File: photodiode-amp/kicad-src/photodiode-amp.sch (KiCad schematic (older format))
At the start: 10 parts, among them J2 Conn_01x04, U1 OPA333xxDBV

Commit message: creates pd amp prod files
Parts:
- gave numbers to parts that had none: 1
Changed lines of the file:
@@
 $EndComp
 $Comp
-L Sensor_Optical:BPX61 D?
+L Sensor_Optical:BPX61 D1
 U 1 1 61B6A38B
 P 5325 2575
-F 0 "D?" V 5321 2497 50  0000 R CNN
+F 0 "D1" V 5321 2497 50  0000 R CNN
 F 1 "BPX61" V 5230 2497 50  0000 R CNN
 F 2 "Package_TO_SOT_THT:TO-5-2_Window" H 5325 2750 50  0001 C CNN

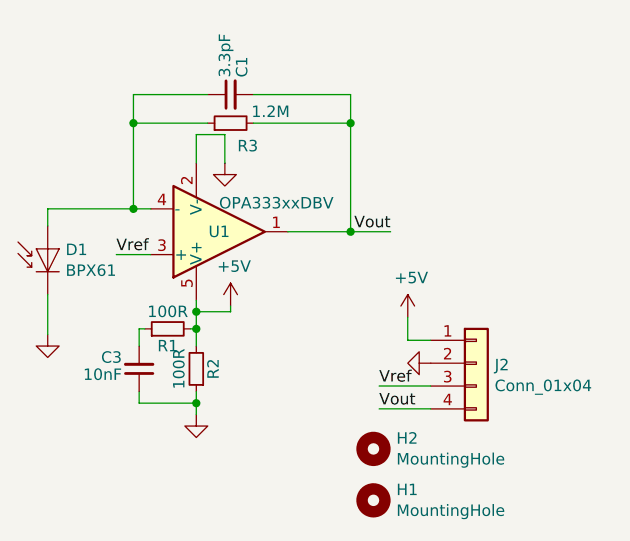
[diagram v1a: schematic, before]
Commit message: update component values and ids
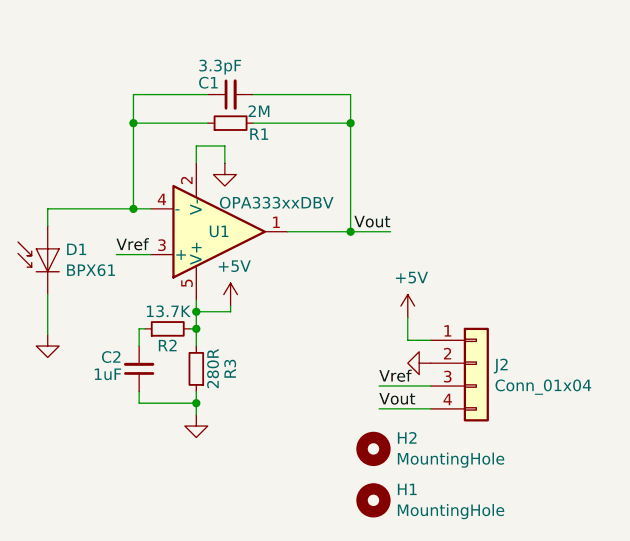
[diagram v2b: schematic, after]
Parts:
- C2: renamed from C3; value 10nF -> 1uF
- R1: renamed from R3; value 1.2M -> 2M
- R2: renamed from R1; value 100R -> 13.7K
- R3: renamed from R2; value 100R -> 280R
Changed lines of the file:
@@
 $EndDescr
 $Comp
-L Device:R_Small R2
+L Device:R_Small R3
 U 1 1 61AFAEA8
 P 5975 3100
-F 0 "R2" V 5900 3100 50  0000 C CNN
-F 1 "100R" V 6050 3100 50  0000 C CNN
+F 0 "R3" V 5825 3100 50  0000 C CNN
+F 1 "280R" V 5900 3100 50  0000 C CNN
 F 2 "Resistor_SMD:R_0603_1608Metric" H 5975 3100 50  0001 C CNN
 F 3 "~" H 5975 3100 50  0001 C CNN
@@
 	5975 2800 5975 2850
 $Comp
-L Device:C_Small C3
+L Device:C_Small C2
 U 1 1 61A9D282
 P 5725 3100
-F 0 "C3" H 5800 3050 50  0000 L CNN
-F 1 "10nF" H 5800 3125 50  0000 L CNN
+F 0 "C2" H 5800 3050 50  0000 L CNN
+F 1 "1uF" H 5800 3125 50  0000 L CNN
 F 2 "Capacitor_SMD:C_0603_1608Metric" H 5725 3100 50  0001 C CNN
 F 3 "~" H 5725 3100 50  0001 C CNN
@@
 $EndComp
 $Comp
-L Device:R_Small R1
+L Device:R_Small R2
 U 1 1 61B2103D
 P 5850 2925
-F 0 "R1" V 5775 2925 50  0000 C CNN
-F 1 "100R" V 5925 2925 50  0000 C CNN
+F 0 "R2" V 5775 2925 50  0000 C CNN
+F 1 "13.7K" V 5925 2925 50  0000 C CNN
 F 2 "Resistor_SMD:R_0603_1608Metric" H 5850 2925 50  0001 C CNN
 F 3 "~" H 5850 2925 50  0001 C CNN
@@
 U 1 1 61B23471
 P 6125 1900
-F 0 "C1" H 6200 1850 50  0000 L CNN
-F 1 "3.3pF" H 6200 1925 50  0000 L CNN
+F 0 "C1" V 6175 1950 50  0000 L CNN
+F 1 "3.3pF" V 6250 1850 50  0000 L CNN
 F 2 "Capacitor_SMD:C_0603_1608Metric" H 6125 1900 50  0001 C CNN
 F 3 "~" H 6125 1900 50  0001 C CNN
@@
 $EndComp
 Wire Wire Line
-	6100 2200 6100 2075
+	6100 2200 6100 2125
 Wire Wire Line
-	6100 2075 5975 2075
+	6100 2125 5975 2125
 Wire Wire Line
-	5975 2075 5975 2200
+	5975 2125 5975 2200
 $Comp
-L Device:R_Small R3
+L Device:R_Small R1
 U 1 1 61B275EE
 P 6125 2025
-F 0 "R3" V 6025 1950 50  0000 C CNN
-F 1 "1.2M" V 6175 1850 50  0000 C CNN
+F 0 "R1" V 6075 1900 50  0000 C CNN
+F 1 "2M" V 6175 1900 50  0000 C CNN
 F 2 "Resistor_SMD:R_0603_1608Metric" H 6125 2025 50  0001 C CNN
 F 3 "~" H 6125 2025 50  0001 C CNN
